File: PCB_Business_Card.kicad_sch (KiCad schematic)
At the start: 4 parts, among them U1 NT3H1101W0FTTJ

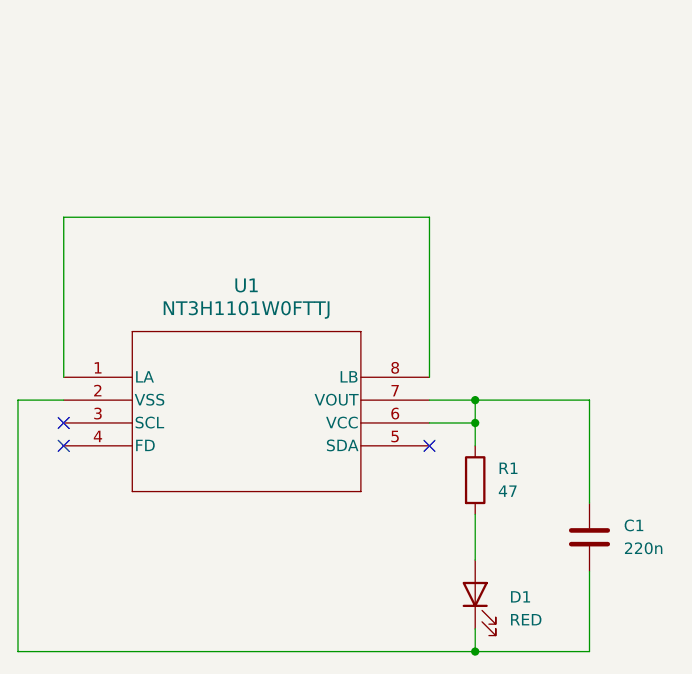
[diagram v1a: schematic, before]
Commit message: Added tuning capacitor
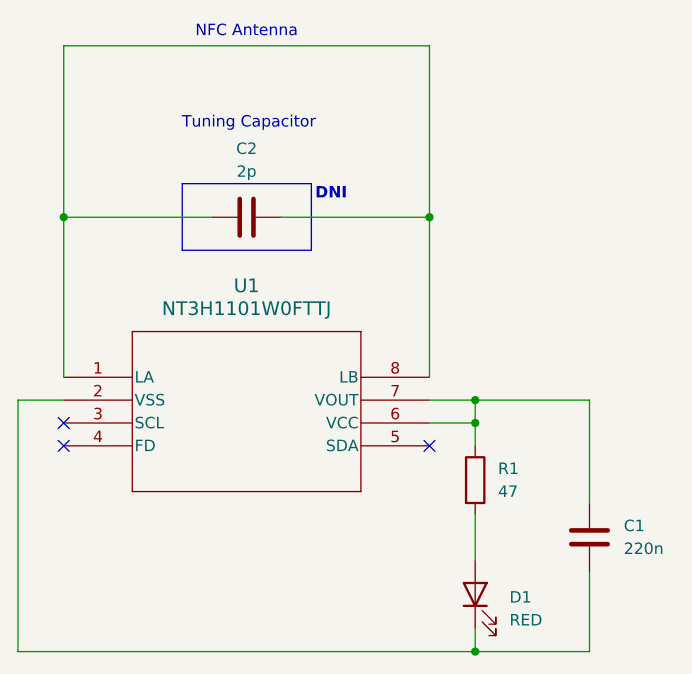
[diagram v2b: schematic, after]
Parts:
- added C2: 2p, Capacitor_SMD:C_0603_1608Metric, symbol Device:C
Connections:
- net at U1.1 (LA), U1.8 (LB): now also C2.1, C2.2
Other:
- note added: "DNI"
- note added: "NFC Antenna"
- note added: "Tuning Capacitor"
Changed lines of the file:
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@@
+	)
+	(junction
+		(at 119.38 76.2)
+		(diameter 0)
+		(color 0 0 0 0)
 	)
 	(junction
@@
 		(color 0 0 0 0)
 	)
+	(junction
+		(at 160.02 76.2)
+		(diameter 0)
+		(color 0 0 0 0)
+	)
 	(no_connect
 		(at 119.38 101.6)
@@
 	(wire
 		(pts
-			(xy 119.38 76.2) (xy 160.02 76.2)
+			(xy 160.02 57.15) (xy 160.02 76.2)
+		)
+		(stroke
+			(width 0)
+			(type default)
+		)
+	)
+	(wire
+		(pts
+			(xy 143.51 76.2) (xy 160.02 76.2)
+		)
+		(stroke
+			(width 0)
+			(type default)
+		)
+	)
+	(wire
+		(pts
+			(xy 119.38 57.15) (xy 160.02 57.15)
 		)
 		(stroke
@@
 	(wire
 		(pts
+			(xy 119.38 76.2) (xy 119.38 57.15)
+		)
+		(stroke
+			(width 0)
+			(type default)
+		)
+	)
+	(wire
+		(pts
 			(xy 165.1 96.52) (xy 177.8 96.52)
 		)
@@
 	(wire
 		(pts
+			(xy 119.38 76.2) (xy 135.89 76.2)
+		)
+		(stroke
+			(width 0)
+			(type default)
+		)
+	)
+	(wire
+		(pts
 			(xy 177.8 115.57) (xy 177.8 124.46)
 		)
@@
 			(width 0)
 			(type default)
+		)
+	)
+	(rectangle
+		(start 132.5499 72.4662)
+		(end 146.9009 79.8703)
+		(stroke
+			(width 0)
+			(type default)
+		)
+		(fill
+			(type none)
+		)
+	)
+	(text "DNI"
+		(exclude_from_sim no)
+		(at 149.098 73.66 0)
+		(effects
+			(font
+				(size 1.27 1.27)
+				(thickness 0.254)
+				(bold yes)
+			)
+		)
+	)
+	(text "NFC Antenna"
+		(exclude_from_sim no)
+		(at 139.7 55.626 0)
+		(effects
+			(font
+				(size 1.27 1.27)
+			)
+		)
+	)
+	(text "Tuning Capacitor"
+		(exclude_from_sim no)
+		(at 139.954 65.786 0)
+		(effects
+			(font
+				(size 1.27 1.27)
+			)
 		)
 	)
@@
 					(unit 1)
 				)
+			)
+		)
+	)
+	(symbol
+		(lib_id "Device:C")
+		(at 139.7 76.2 90)
+		(unit 1)
+		(exclude_from_sim no)
+		(in_bom yes)
+		(on_board yes)
+		(dnp no)
+		(fields_autoplaced yes)
+		(property "Reference" "C2"
+			(at 139.7 68.58 90)
+			(effects
+				(font
+					(size 1.27 1.27)
+				)
+			)
+		)
+		(property "Value" "2p"
+			(at 139.7 71.12 90)
+			(effects
+				(font
+					(size 1.27 1.27)
+				)
+			)
+		)
+		(property "Footprint" "Capacitor_SMD:C_0603_1608Metric"
+			(at 143.51 75.2348 0)
+			(effects
+				(font
+					(size 1.27 1.27)
+				)
+				(hide yes)
+			)
+		)
+		(property "Datasheet" "~"
+			(at 139.7 76.2 0)
+			(effects
+				(font
+					(size 1.27 1.27)
+				)
+				(hide yes)
+			)
+		)
+		(property "Description" "Unpolarized capacitor"
+			(at 139.7 76.2 0)
+			(effects
+				(font
+					(size 1.27 1.27)
+				)
+				(hide yes)
+			)
+		)
+		(pin "1"
+		)
+		(pin "2"
+		)
+		(instances
+			(project "PCB_Business_Card"
+				(path "/9044140f-1e15-4de5-8f54-dc011c7b5494"
+					(reference "C2")
+					(unit 1)
+				)

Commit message: Circuit Response
* Network analyzer graph
* Spectrum analyzer graph
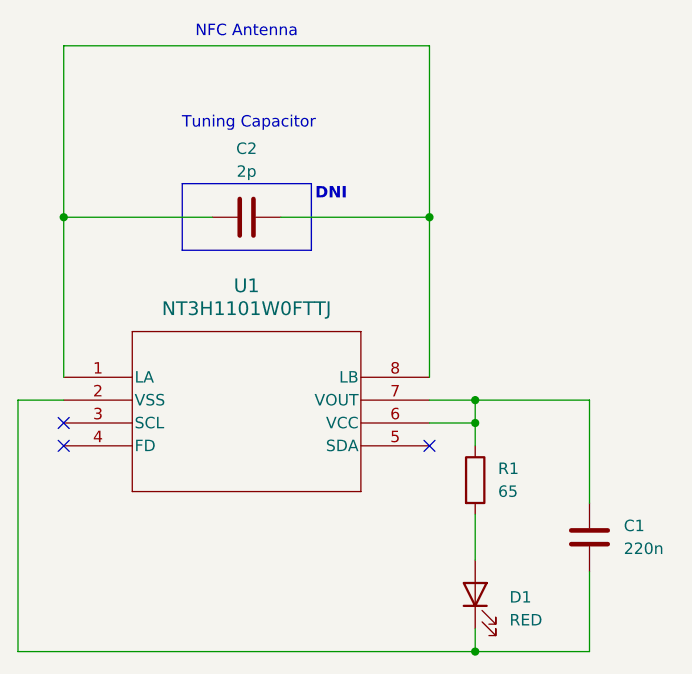
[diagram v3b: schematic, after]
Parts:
- R1: value 47 -> 65
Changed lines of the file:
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@@
 			)
 		)
-		(property "Value" "47"
+		(property "Value" "65"
 			(at 167.64 106.6799 0)
 			(effects
